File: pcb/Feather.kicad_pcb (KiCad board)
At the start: 2 copper layers, 52.6 x 22.9 mm, 39 parts, among them J1 10118192, J2 S2B-PH-SM4-TB, J3 ANT, J4 U.FL-R-SMT-1, J5 Conn_01x03, J6 Conn_01x12, J7 Conn_01x16, SW1 KMR2, U1 ATSAMD21G18A-M, U2 AP2112K-3.3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

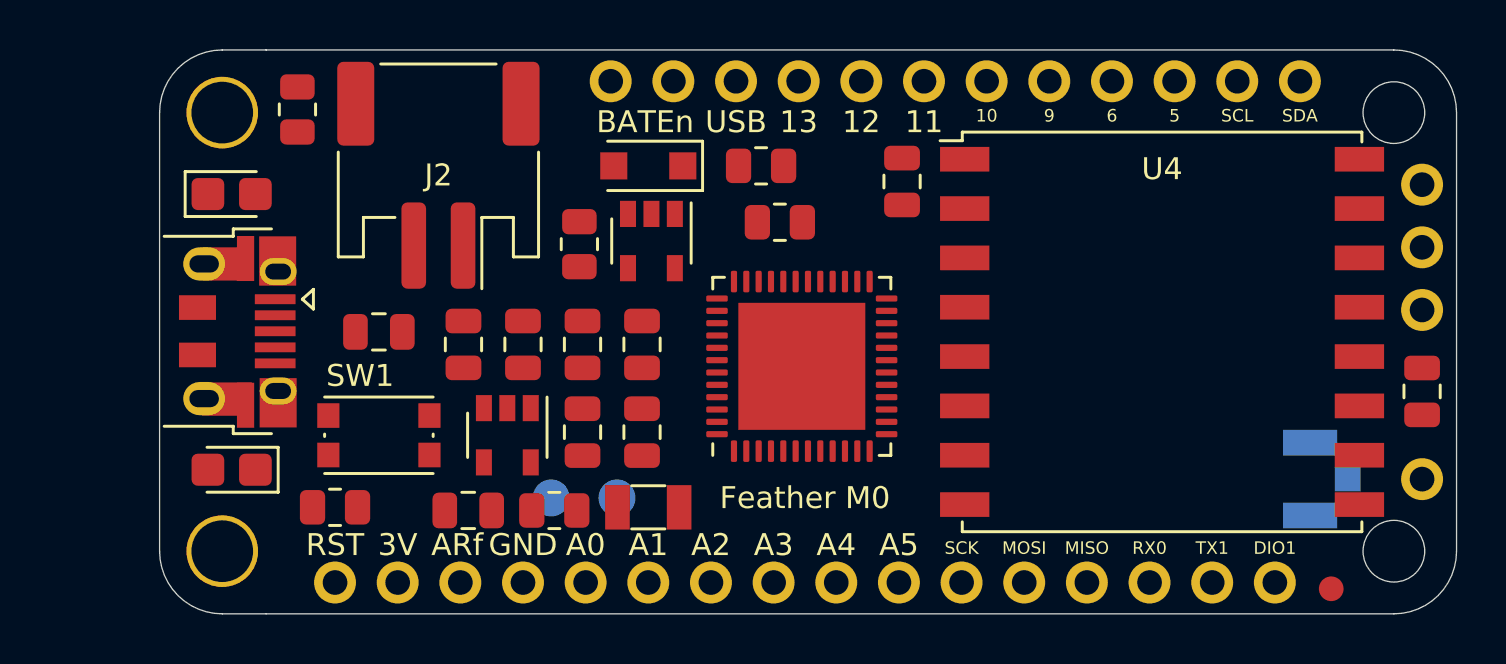
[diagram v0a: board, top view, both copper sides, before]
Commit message: Se hicieron más ajustes para acomodar mejor los componentes tamaño 0805 no contemplados al comienzo del posicionamiento.
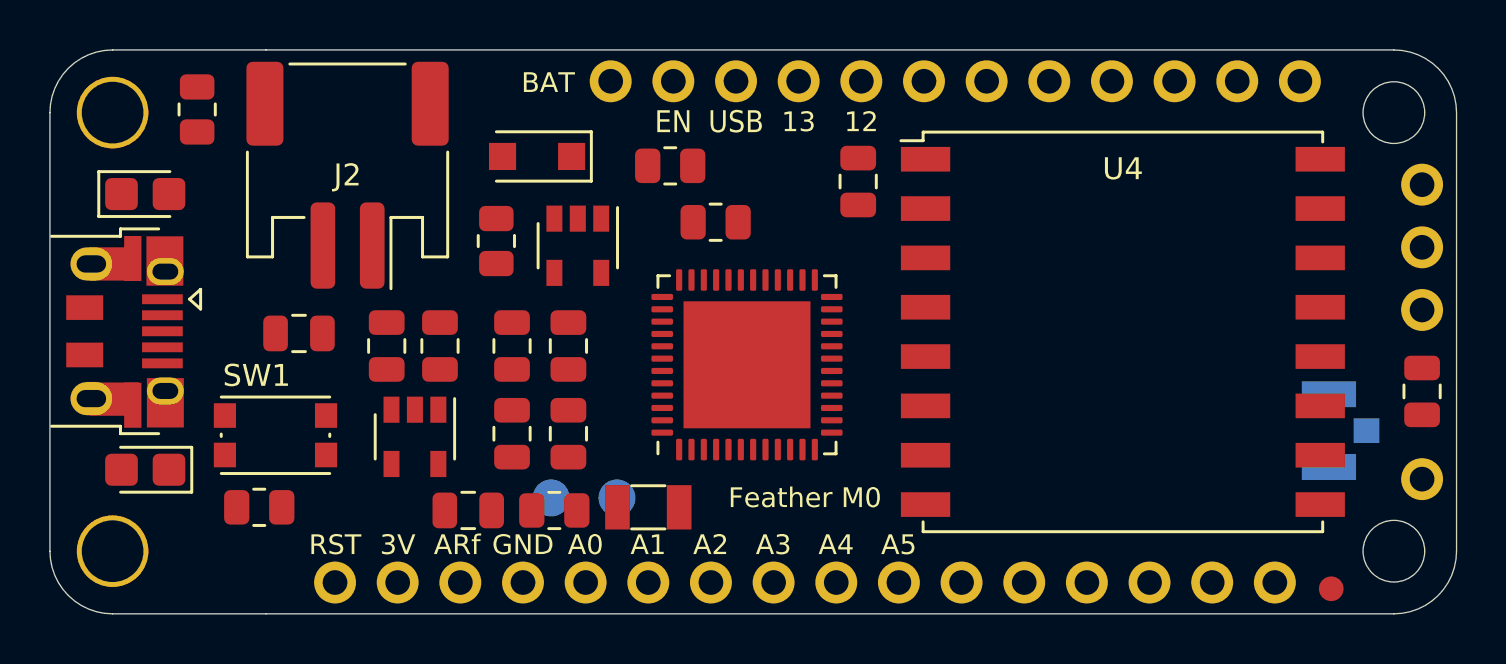
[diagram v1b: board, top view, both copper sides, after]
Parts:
- moved J1 4.57 mm to (117.0, 90.9)
- moved D1 4.52 mm to (133.9, 83.8)
- moved H1 4.45 mm to (116.7, 82.0)
- moved H3 4.45 mm to (116.7, 99.8)
- moved SW1 4.19 mm to (123.3, 95.1)
- moved R7 4.06 mm to (120.1, 81.9)
- moved U3 3.75 mm to (129.0, 95.2)
- moved R5 3.68 mm to (139.3, 84.2)
- moved J2 3.68 mm to (126.2, 84.6)
- moved D2 3.50 mm to (118.0, 96.5)
- moved D3 3.50 mm to (118.0, 85.3)
- moved R1 3.37 mm to (132.3, 87.2)
- moved C6 3.37 mm to (130.0, 91.5)
- moved C5 3.24 mm to (124.3, 91.0), turned to 0 degrees
- moved C9 3.11 mm to (127.8, 91.5)
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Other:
- board size 52.6 x 22.9 mm -> 57 x 22.9 mm
- rule pad_to_mask_clearance: 0 -> 0.2
- board text added: "1) Grid size: 0,127 mm (5 mils)."
- board text added: "2) Minimum clearance: 0,2 mm (7,87 mils)."
- board text added: "3) Minimum via size: 0,8 mm/0,4 mm (31,5 mils/15,74 mils)."
- board text added: "4) Minimum track size: 0,2 mm (7,87 mils)."
- board text added: "5) Designed according to Mayer Circuitos Impresos fabrication capabilities."
- board text added: "6) It was required to use 0805 as the minimum acceptable size for all components. For that reason, this design is 6,223 mm longer that the original desing."
- board text added: "7) PCB size may be subject to change after the routing process starts."
- board text added: "8) For compatibility reasons, PCB height can't be modified."
- board text added: "BAT"
- board text added: "EN"
- board text added: "Surface finish: HASL Soldermask color: Black Silkscreen color: White"
- board text removed: "1) Grid size: 0,127 mm (5 mils)"
- board text removed: "2) It was required to use 0805 as the minimum acceptable size for all components. For that reason, this design is 1,768 mm longer that the original desing."
- board text removed: "3) PCB size may be subject to change based after the routing process starts."
- board text removed: "BATEn"
- board text removed: "Surface finish: HASL Silkscreen color: Black"
